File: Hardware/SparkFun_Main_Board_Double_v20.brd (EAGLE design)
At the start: 124.5 x 73.7 mm, 134 parts, among them J1 MICROMOD-2222-C, J10 MICRO-SD-PUSH-PUSH-EXT-PIN, J2 Vertical Qwiic Connector, J4 QWIIC_RIGHT_ANGLE, J5 CORTEX_JTAG_DEBUG_MINIMUM_PTH, J6 MICROMOD_FUNCTION_MAIN, J7 MICROMOD_FUNCTION_MAIN, Q1 3.1A/30V/105mΩ, Q2 20V/4.2A/52mΩ/1.4W, U1 STG3856QTR, U2 MCP73831, U3 ESD Diode, U4 AP7347DQ-33W5-7K-3.3V, U5 AP7361C-33

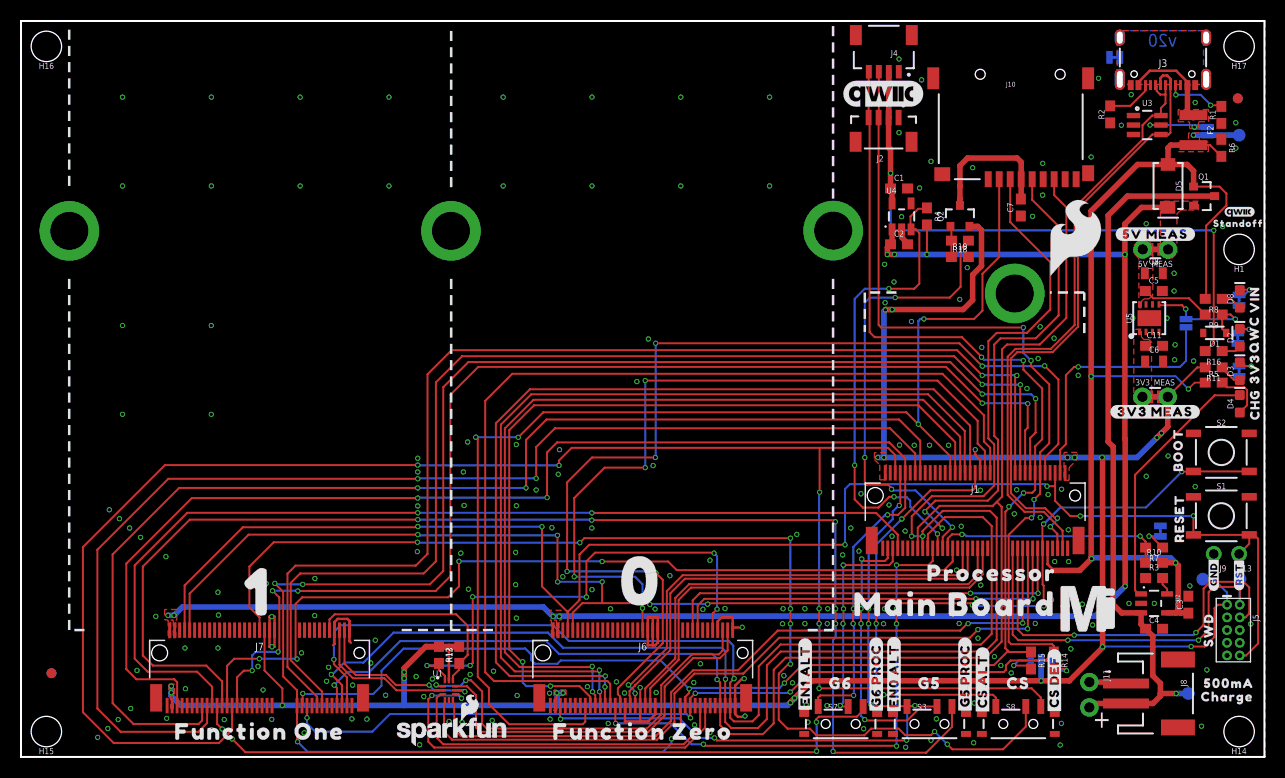
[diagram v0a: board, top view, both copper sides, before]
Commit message: Moves I2C pullups to make space for silk
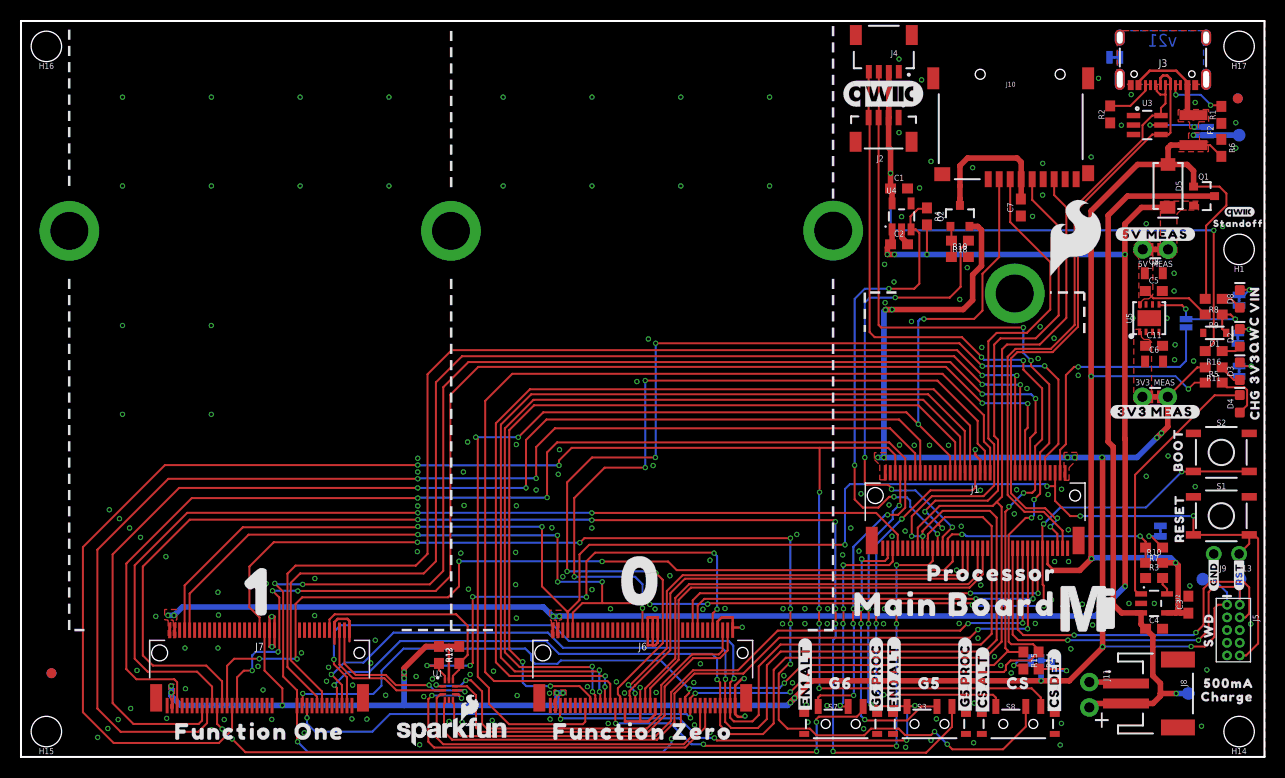
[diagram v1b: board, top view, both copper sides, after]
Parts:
- moved R14 1.52 mm to (101.9, 9.65)
- moved R15 0.76 mm to (100.3, 9.65)
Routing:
- net I2C_SDA: track 161.7 -> 158.5 mm
- net N$11: track 3.74 -> 5.26 mm
- net N$13: track 3.78 -> 3.02 mm
- net I2C_SCL: track 157.4 -> 156.7 mm
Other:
- board text added: "v21"
- board text removed: "v20"
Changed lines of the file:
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@@
 <layer number="37" name="tTest" color="7" fill="1" visible="no" active="yes"/>
 <layer number="38" name="bTest" color="7" fill="1" visible="no" active="yes"/>
-<layer number="39" name="tKeepout" color="4" fill="11" visible="no" active="yes"/>
+<layer number="39" name="tKeepout" color="4" fill="11" visible="yes" active="yes"/>
 <layer number="40" name="bKeepout" color="1" fill="11" visible="no" active="yes"/>
 <layer number="41" name="tRestrict" color="4" fill="10" visible="no" active="yes"/>
@@
 <wire x1="0" y1="0" x2="0" y2="73.66" width="0.2032" layer="20"/>
 <wire x1="124.46" y1="0" x2="124.46" y2="73.66" width="0.2032" layer="20"/>
-<text x="114.2492" y="71.7296" size="1.27" layer="16" font="vector" ratio="15" rot="MR180" align="center">v20</text>
+<text x="114.2492" y="71.7296" size="1.27" layer="16" font="vector" ratio="15" rot="MR180" align="center">v21</text>
 <text x="63.5" y="-24.384" size="1.778" layer="51" font="vector">Elias Santistevan</text>
 <text x="-0.127" y="-12.319" size="1.778" layer="47" font="vector" ratio="15" rot="R180">Units in Inches</text>
@@
 <attribute name="VALUE" x="102.108" y="10.795" size="0.6096" layer="28" font="vector" ratio="20" rot="MR180" align="top-center"/>
 </element>
-<element name="R14" library="SparkFun-Resistors" package="0603" value="2.2k" x="103.378" y="9.652" smashed="yes" rot="R270">
-<attribute name="NAME" x="104.14" y="9.652" size="0.6096" layer="25" font="vector" ratio="20" rot="R270" align="bottom-center"/>
-<attribute name="PROD_ID" value="RES-08272" x="103.378" y="9.652" size="1.778" layer="27" font="vector" ratio="15" rot="R270" display="off"/>
-<attribute name="VALUE" x="102.616" y="9.652" size="0.6096" layer="27" font="vector" ratio="20" rot="R270" align="top-center"/>
-</element>
-<element name="R15" library="SparkFun-Resistors" package="0603" value="2.2k" x="101.092" y="9.652" smashed="yes" rot="R270">
-<attribute name="NAME" x="101.854" y="9.652" size="0.6096" layer="25" font="vector" ratio="20" rot="R270" align="bottom-center"/>
-<attribute name="PROD_ID" value="RES-08272" x="101.092" y="9.652" size="1.778" layer="27" font="vector" ratio="15" rot="R270" display="off"/>
-<attribute name="VALUE" x="100.33" y="9.652" size="0.6096" layer="27" font="vector" ratio="20" rot="R270" align="top-center"/>
+<element name="R14" library="SparkFun-Resistors" package="0603" value="2.2k" x="101.854" y="9.652" smashed="yes" rot="R270">
+<attribute name="NAME" x="102.616" y="9.652" size="0.6096" layer="25" font="vector" ratio="20" rot="R270" align="bottom-center"/>
+<attribute name="PROD_ID" value="RES-08272" x="101.854" y="9.652" size="1.778" layer="27" font="vector" ratio="15" rot="R270" display="off"/>
+<attribute name="VALUE" x="101.092" y="9.652" size="0.6096" layer="27" font="vector" ratio="20" rot="R270" align="top-center"/>
+</element>
+<element name="R15" library="SparkFun-Resistors" package="0603" value="2.2k" x="100.33" y="9.652" smashed="yes" rot="R270">
+<attribute name="NAME" x="101.092" y="9.652" size="0.6096" layer="25" font="vector" ratio="20" rot="R270" align="bottom-center"/>
+<attribute name="PROD_ID" value="RES-08272" x="100.33" y="9.652" size="1.778" layer="27" font="vector" ratio="15" rot="R270" display="off"/>
+<attribute name="VALUE" x="99.568" y="9.652" size="0.6096" layer="27" font="vector" ratio="20" rot="R270" align="top-center"/>
 </element>
 <element name="U$20" library="top" package="#CS_ALT#20" value="" x="96.2406" y="7.5946" smashed="yes" rot="R90"/>
@@
 <wire x1="32.876" y1="13.606" x2="32.6644" y2="13.8176" width="0.254" layer="1"/>
 <wire x1="31.376" y1="12.689" x2="31.376" y2="11.31" width="0.254" layer="1"/>
-<wire x1="31.376" y1="11.31" x2="31.242" y2="11.176" width="0.254" layer="1"/>
 <wire x1="32.876" y1="12.689" x2="32.876" y2="11.574" width="0.254" layer="1"/>
-<wire x1="32.876" y1="11.574" x2="33.02" y2="11.43" width="0.254" layer="1"/>
 <wire x1="71.48" y1="5.139" x2="71.48" y2="7.1418" width="0.254" layer="1"/>
 <via x="72.4662" y="4.0894" extent="1-16" drill="0.3048"/>
@@
 <wire x1="98.5266" y1="10.886825" x2="98.7757125" y2="10.6377125" width="0.2032" layer="1"/>
 <wire x1="98.7757125" y1="10.6377125" x2="98.911425" y2="10.502" width="0.2032" layer="1"/>
-<wire x1="98.911425" y1="10.502" x2="101.092" y2="10.502" width="0.2032" layer="1"/>
+<wire x1="98.911425" y1="10.502" x2="100.33" y2="10.502" width="0.2032" layer="1"/>
 <wire x1="98.5266" y1="24.5364" x2="98.5266" y2="10.886825" width="0.2032" layer="1"/>
 <wire x1="98.7757125" y1="10.6377125" x2="98.7757125" y2="10.5869125" width="0.2032" layer="1"/>
@@
 <wire x1="35.179" y1="2.54" x2="29.4386" y2="2.54" width="0.2032" layer="16"/>
 <wire x1="36.9316" y1="4.2926" x2="35.179" y2="2.54" width="0.2032" layer="16"/>
-<wire x1="103.378" y1="11.1132875" x2="103.378" y2="10.502" width="0.2032" layer="1"/>
-<wire x1="103.2106875" y1="11.2806" x2="103.378" y2="11.1132875" width="0.2032" layer="1"/>
-<wire x1="98.8568" y1="11.5316" x2="99.1078" y2="11.2806" width="0.2032" layer="1"/>
-<wire x1="99.1078" y1="11.2806" x2="103.2106875" y2="11.2806" width="0.2032" layer="1"/>
-<wire x1="103.378" y1="10.502" x2="102.528" y2="9.652" width="0.2032" layer="1"/>
-<wire x1="102.528" y1="9.652" x2="99.06" y2="9.652" width="0.2032" layer="1"/>
+<wire x1="99.1078" y1="11.2806" x2="98.8568" y2="11.5316" width="0.2032" layer="1"/>
+<wire x1="101.854" y1="10.502" x2="101.004" y2="9.652" width="0.2032" layer="1"/>
+<wire x1="101.004" y1="9.652" x2="99.06" y2="9.652" width="0.2032" layer="1"/>
 <wire x1="99.06" y1="9.652" x2="98.5774" y2="9.1694" width="0.2032" layer="1"/>
 <wire x1="98.5774" y1="8.7122" x2="98.3615" y2="8.4963" width="0.2032" layer="1"/>
@@
 <via x="101.3968" y="25.7556" extent="1-16" drill="0.3048"/>
 <wire x1="101.3968" y1="25.7556" x2="102.004" y2="26.3628" width="0.2032" layer="1"/>
+<wire x1="101.854" y1="10.502" x2="101.854" y2="10.7322875" width="0.2032" layer="1"/>
+<wire x1="101.854" y1="10.7322875" x2="101.3056875" y2="11.2806" width="0.2032" layer="1"/>
+<wire x1="101.3056875" y1="11.2806" x2="99.1078" y2="11.2806" width="0.2032" layer="1"/>
 </signal>
 <signal name="HOST_D-" class="2">
@@
 <contactref element="I2C_PU" pad="3"/>
 <contactref element="R14" pad="2"/>
-<wire x1="103.378" y1="8.802" x2="104.482" y2="8.802" width="0.2032" layer="1"/>
+<wire x1="101.854" y1="8.802" x2="104.482" y2="8.802" width="0.2032" layer="1"/>
 <wire x1="104.482" y1="8.802" x2="104.648" y2="8.636" width="0.2032" layer="1"/>
 <via x="104.648" y="8.636" extent="1-16" drill="0.3048"/>
@@
 <contactref element="I2C_PU" pad="1"/>
 <contactref element="R15" pad="2"/>
-<wire x1="101.092" y1="8.802" x2="100.75" y2="9.144" width="0.2032" layer="1"/>
-<wire x1="100.75" y1="9.144" x2="99.3648" y2="9.144" width="0.2032" layer="1"/>
+<wire x1="100.33" y1="8.802" x2="99.988" y2="9.144" width="0.2032" layer="1"/>
+<wire x1="99.988" y1="9.144" x2="99.3648" y2="9.144" width="0.2032" layer="1"/>
 <via x="99.3648" y="9.144" extent="1-16" drill="0.3048"/>
 <wire x1="99.3648" y1="9.144" x2="99.8728" y2="9.652" width="0.2032" layer="16"/>
